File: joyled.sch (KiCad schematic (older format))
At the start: 16 parts, among them P3 GAMEPAD 2, P6 GAMEPAD 1, U1 VGA SYNC/JOY BUFFER, U7 BACKLIGHT COVER

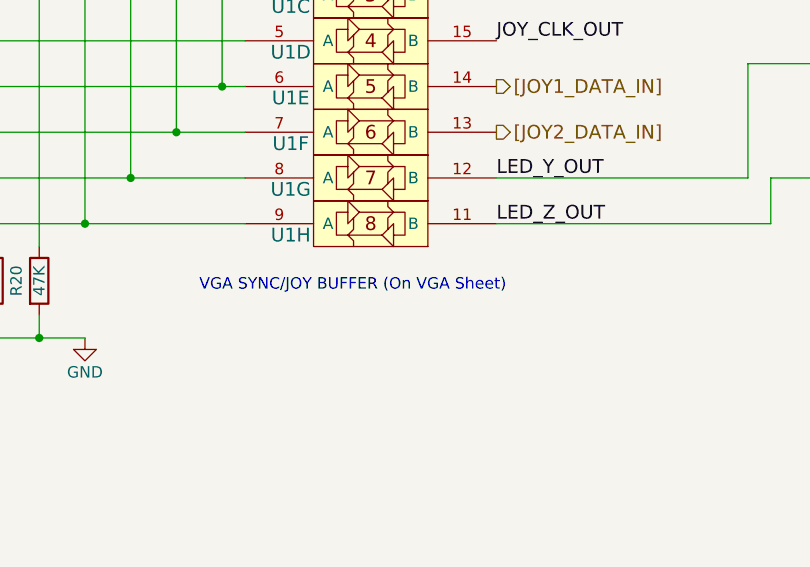
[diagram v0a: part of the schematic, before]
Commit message: Detalles menores (reordenamiento de labels, correccion de titulo, etc
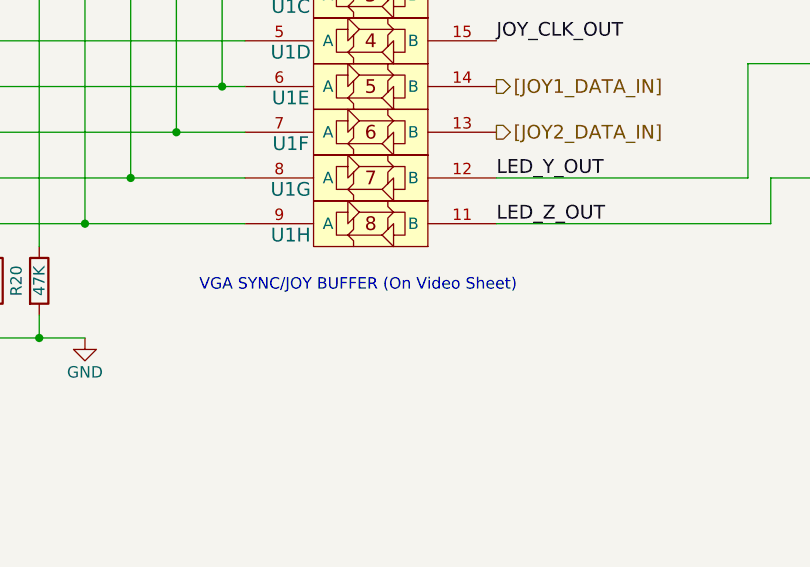
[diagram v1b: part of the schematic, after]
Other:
- note added: "VGA SYNC/JOY BUFFER (On Video Sheet)"
- note removed: "VGA SYNC/JOY BUFFER (On VGA Sheet)"
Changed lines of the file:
@@
 Connection ~ 2400 2600
 Text Notes 3300 3700 0    50   ~ 0
-VGA SYNC/JOY BUFFER (On VGA Sheet)
+VGA SYNC/JOY BUFFER (On Video Sheet)
 $Comp
 L DB9S_NES8 P3

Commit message: Cambios menores
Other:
- moved on the sheet: G3, G4
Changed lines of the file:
@@
 $EndComp
 $Comp
-L GND #PWR022
+L GND #PWR019
 U 1 1 5BD0B1F1
 P 2800 3900
-F 0 "#PWR022" H 2800 3650 50  0001 C CNN
+F 0 "#PWR019" H 2800 3650 50  0001 C CNN
 F 1 "GND" H 2800 3750 50  0000 C CNN
 F 2 "" H 2800 3900 50  0000 C CNN
@@
 $EndComp
 $Comp
-L +3.3V #PWR023
+L +3.3V #PWR020
 U 1 1 5BD0B1F7
 P 2200 1900
-F 0 "#PWR023" H 2200 1750 50  0001 C CNN
+F 0 "#PWR020" H 2200 1750 50  0001 C CNN
 F 1 "+3.3V" H 2200 2040 50  0000 C CNN
 F 2 "" H 2200 1900 50  0000 C CNN
@@
 LED_Z_OUT
 $Comp
-L +5V #PWR024
+L +5V #PWR021
 U 1 1 5BD0B238
 P 7400 2700
-F 0 "#PWR024" H 7400 2550 50  0001 C CNN
+F 0 "#PWR021" H 7400 2550 50  0001 C CNN
 F 1 "+5V" H 7400 2840 50  0000 C CNN
 F 2 "" H 7400 2700 50  0000 C CNN
@@
 $EndComp
 $Comp
-L +5V #PWR025
+L +5V #PWR022
 U 1 1 5BD0B23E
 P 7400 3200
-F 0 "#PWR025" H 7400 3050 50  0001 C CNN
+F 0 "#PWR022" H 7400 3050 50  0001 C CNN
 F 1 "+5V" H 7400 3340 50  0000 C CNN
 F 2 "" H 7400 3200 50  0000 C CNN
@@
 L INVADER_LOGO_BACK G3
 U 1 1 5BD0B291
-P 5225 5475
-F 0 "G3" H 5225 5650 60  0000 C CNN
-F 1 "LOGO BACKLIGHT" H 5225 5150 60  0000 C CNN
-F 2 "Salmon:TREX_LOGO_BACK" H 5225 5475 60  0001 C CNN
-F 3 "" H 5225 5475 60  0001 C CNN
-	1    5225 5475
+P 5725 5475
+F 0 "G3" H 5725 5650 60  0000 C CNN
+F 1 "LOGO BACKLIGHT" H 5725 5150 60  0000 C CNN
+F 2 "Salmon:TREX_LOGO_BACK" H 5725 5475 60  0001 C CNN
+F 3 "" H 5725 5475 60  0001 C CNN
+	1    5725 5475
 	1    0    0    -1
 $EndComp
@@
 L RETROCIAA_LOGO_BACK G4
 U 1 1 5BD0B298
-P 3850 5475
-F 0 "G4" H 3850 5650 60  0000 C CNN
-F 1 "RETRO-CIAA BACKLIGHT" H 3850 5150 60  0000 C CNN
-F 2 "Salmon:RETROCIAA_LOGO_BACK" H 3850 5475 60  0001 C CNN
-F 3 "" H 3850 5475 60  0001 C CNN
-	1    3850 5475
+P 4050 5475
+F 0 "G4" H 4050 5650 60  0000 C CNN
+F 1 "RETRO-CIAA BACKLIGHT" H 4050 5150 60  0000 C CNN
+F 2 "Salmon:RETROCIAA_LOGO_BACK" H 4050 5475 60  0001 C CNN
+F 3 "" H 4050 5475 60  0001 C CNN
+	1    4050 5475
 	1    0    0    -1
 $EndComp
@@
 NES 8 Bit (Family Game) Gamepads\nusing CMOS 4021 shift register.
 $Comp
-L Earth #PWR026
+L Earth #PWR023
 U 1 1 5BD0EAA8
 P 10500 4100
-F 0 "#PWR026" H 10500 3850 50  0001 C CNN
+F 0 "#PWR023" H 10500 3850 50  0001 C CNN
 F 1 "Earth" H 10500 3950 50  0001 C CNN
 F 2 "" H 10500 4100 50  0000 C CNN
@@
 $EndComp
 $Comp
-L Earth #PWR027
+L Earth #PWR024
 U 1 1 5BD0EAAE
 P 10500 2100
-F 0 "#PWR027" H 10500 1850 50  0001 C CNN
+F 0 "#PWR024" H 10500 1850 50  0001 C CNN
 F 1 "Earth" H 10500 1950 50  0001 C CNN
 F 2 "" H 10500 2100 50  0000 C CNN
@@
 [LED_Z]
 $Comp
-L GND #PWR028
+L GND #PWR025
 U 1 1 5BD2F9D4
 P 1700 5900
-F 0 "#PWR028" H 1700 5650 50  0001 C CNN
+F 0 "#PWR025" H 1700 5650 50  0001 C CNN
 F 1 "GND" H 1700 5750 50  0000 C CNN
 F 2 "" H 1700 5900 50  0000 C CNN
@@
 $EndComp
 $Comp
-L GND #PWR029
+L GND #PWR026
 U 1 1 5BD2FA3A
 P 2700 5900
-F 0 "#PWR029" H 2700 5650 50  0001 C CNN
+F 0 "#PWR026" H 2700 5650 50  0001 C CNN
 F 1 "GND" H 2700 5750 50  0000 C CNN
 F 2 "" H 2700 5900 50  0000 C CNN
@@
 3V3
 $Comp
-L +5V #PWR030
+L +5V #PWR027
 U 1 1 5BD5D879
 P 6100 7400
-F 0 "#PWR030" H 6100 7250 50  0001 C CNN
+F 0 "#PWR027" H 6100 7250 50  0001 C CNN
 F 1 "+5V" H 6100 7540 50  0000 C CNN
 F 2 "" H 6100 7400 50  0000 C CNN
@@
 $EndComp
 $Comp
-L +3.3V #PWR031
+L +3.3V #PWR028
 U 1 1 5BD5D87F
 P 5700 7400
-F 0 "#PWR031" H 5700 7250 50  0001 C CNN
+F 0 "#PWR028" H 5700 7250 50  0001 C CNN
 F 1 "+3.3V" H 5700 7540 50  0000 C CNN
 F 2 "" H 5700 7400 50  0000 C CNN
@@
 $EndComp
 $Comp
-L GND #PWR032
+L GND #PWR029
 U 1 1 5BD5D885
 P 6700 7400
-F 0 "#PWR032" H 6700 7150 50  0001 C CNN
+F 0 "#PWR029" H 6700 7150 50  0001 C CNN
 F 1 "GND" H 6700 7250 50  0000 C CNN
 F 2 "" H 6700 7400 50  0000 C CNN

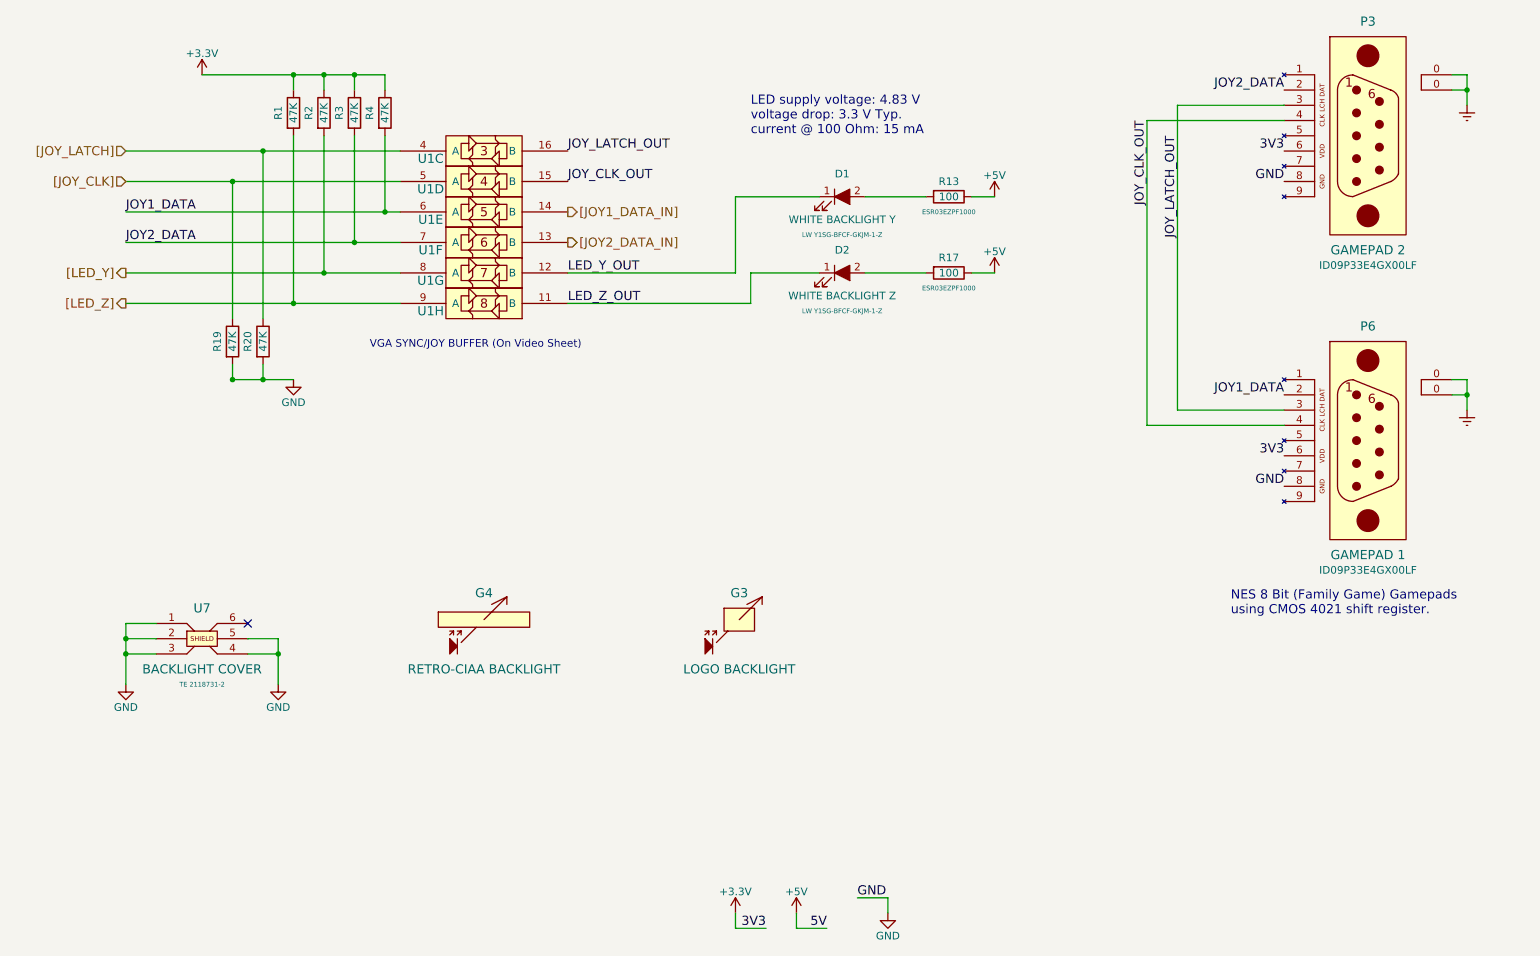
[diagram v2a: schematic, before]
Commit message: Nuevo layout, mejoras y modificaciones del revisor
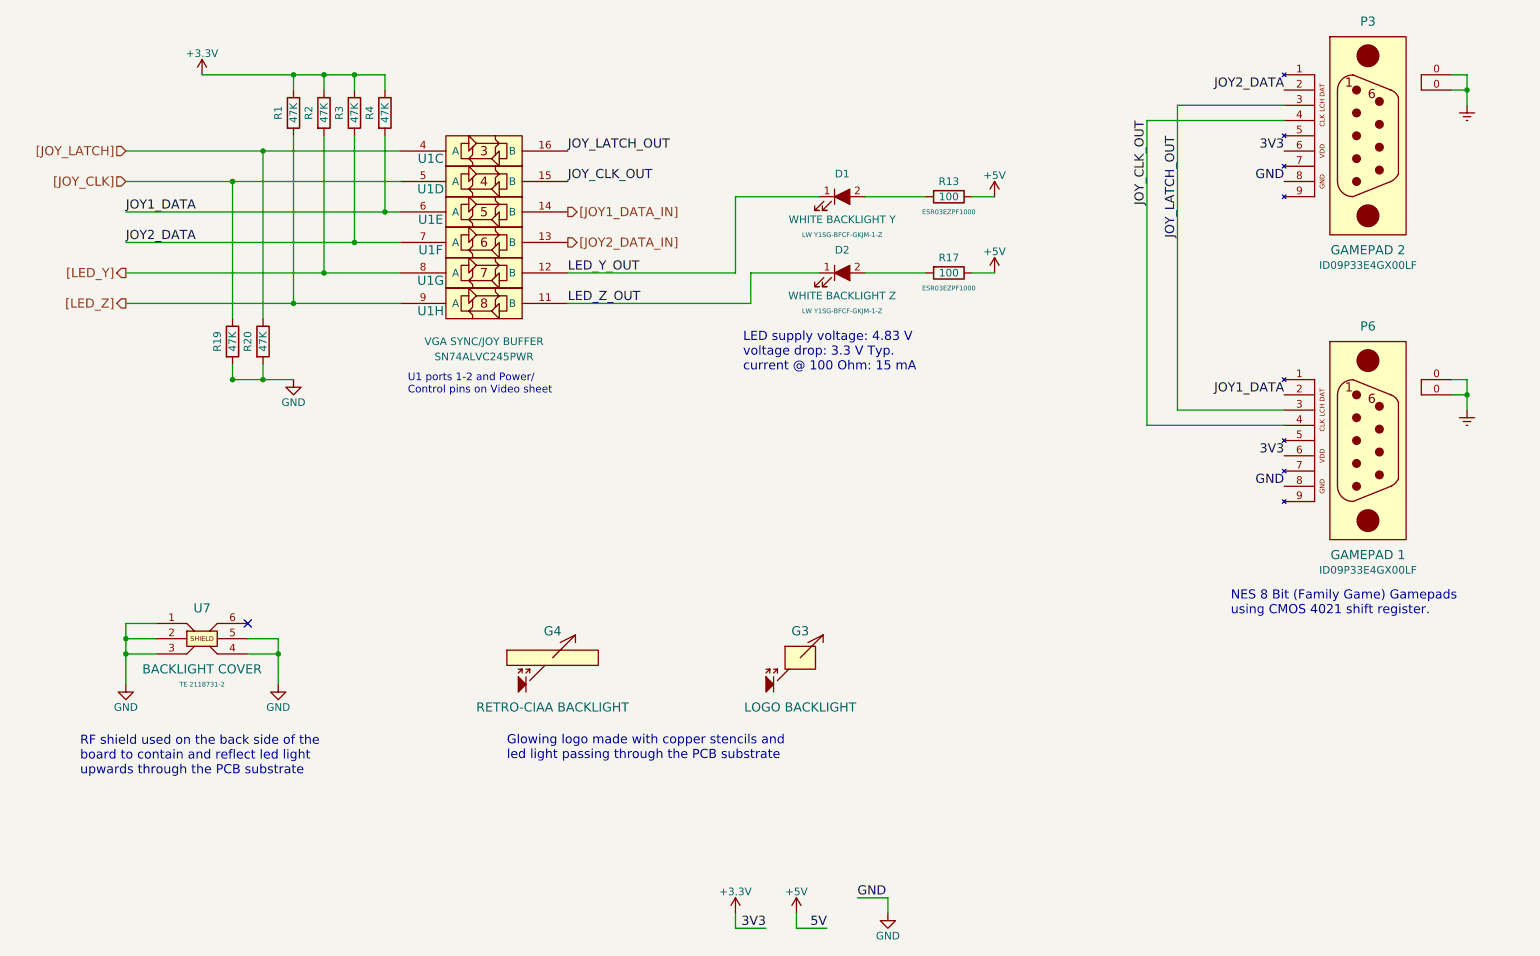
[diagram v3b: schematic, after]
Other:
- note added: "Glowing logo made with copper stencils and\nled light passing through the PCB substrate"
- note added: "RF shield used on the back side of the\nboard to contain and reflect led light \nupwards through the PCB substrate"
- note added: "U1 ports 1-2 and Power/\nControl pins on Video sheet"
- note removed: "VGA SYNC/JOY BUFFER (On Video Sheet)"
- moved on the sheet: G3, G4
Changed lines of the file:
@@
 LIBS:contrib
 LIBS:valves
-LIBS:salmon
+LIBS:retro-ciaa
 LIBS:retro-ciaa-cache
 EELAYER 25 0
@@
 encoding utf-8
 Sheet 3 8
-Title "RETRO-CIAA / JOYSTICKS & BACKLIGHT"
-Date "2018-10-19"
+Title "JOYSTICKS & BACKLIGHT"
+Date "2018-10-20"
 Rev "1.1.1"
-Comp "Salmon Robotics"
+Comp "http://www.retro-ciaa.com"
 Comment1 "All resistors 1% & 0603\" unless otherwise noted"
 Comment2 "ERC check OK on 2018-10-19"
@@
 L INVADER_LOGO_BACK G3
 U 1 1 5BD0B291
-P 5725 5475
-F 0 "G3" H 5725 5650 60  0000 C CNN
-F 1 "LOGO BACKLIGHT" H 5725 5150 60  0000 C CNN
-F 2 "Salmon:TREX_LOGO_BACK" H 5725 5475 60  0001 C CNN
-F 3 "" H 5725 5475 60  0001 C CNN
-	1    5725 5475
+P 6125 5725
+F 0 "G3" H 6125 5900 60  0000 C CNN
+F 1 "LOGO BACKLIGHT" H 6125 5400 60  0000 C CNN
+F 2 "Salmon:TREX_LOGO_BACK" H 6125 5725 60  0001 C CNN
+F 3 "" H 6125 5725 60  0001 C CNN
+	1    6125 5725
 	1    0    0    -1
 $EndComp
@@
 L RETROCIAA_LOGO_BACK G4
 U 1 1 5BD0B298
-P 4050 5475
-F 0 "G4" H 4050 5650 60  0000 C CNN
-F 1 "RETRO-CIAA BACKLIGHT" H 4050 5150 60  0000 C CNN
-F 2 "Salmon:RETROCIAA_LOGO_BACK" H 4050 5475 60  0001 C CNN
-F 3 "" H 4050 5475 60  0001 C CNN
-	1    4050 5475
+P 4500 5725
+F 0 "G4" H 4500 5900 60  0000 C CNN
+F 1 "RETRO-CIAA BACKLIGHT" H 4500 5400 60  0000 C CNN
+F 2 "Salmon:RETROCIAA_LOGO_BACK" H 4500 5725 60  0001 C CNN
+F 3 "" H 4500 5725 60  0001 C CNN
+	1    4500 5725
 	1    0    0    -1
 $EndComp
@@
 AR Path="/5BD08AB9/5BD0C08A" Ref="U1"  Part="8"
 F 0 "U1" H 3700 3350 60  0000 C CNN
-F 1 "VGA SYNC/JOY BUFFER" H 4050 3650 60  0001 C CNN
+F 1 "VGA SYNC/JOY BUFFER" H 4050 3150 50  0000 C CNN
 F 2 "" H 4050 3450 60  0001 C CNN
-F 3 "" H 4050 3450 60  0001 C CNN
+F 3 "SN74ALVC245PWR" H 4050 3050 50  0000 C CNN
 	8    4050 3400
 	1    0    0    -1
@@
 Connection ~ 2600 2400
 Connection ~ 2400 2600
-Text Notes 3300 3700 0    50   ~ 0
-VGA SYNC/JOY BUFFER (On Video Sheet)
+Text Notes 3550 4000 0    50   ~ 0
+U1 ports 1-2 and Power/\nControl pins on Video sheet
 $Comp
 L DB9S_NES8 P3
@@
 Wire Wire Line
 	10500 1900 10400 1900
-Text Notes 5800 2300 0    60   ~ 0
+Text Notes 5750 3850 0    60   ~ 0
 LED supply voltage: 4.83 V\nvoltage drop: 3.3 V Typ.\ncurrent @ 100 Ohm: 15 mA
 Text HLabel 1700 2400 0    60   Input ~ 0
@@
 Text HLabel 4600 3000 2    60   Output ~ 0
 [JOY2_DATA_IN]
+Text Notes 1400 6500 0    60   ~ 0
+RF shield used on the back side of the\nboard to contain and reflect led light \nupwards through the PCB substrate
+Text Notes 4200 6400 0    60   ~ 0
+Glowing logo made with copper stencils and\nled light passing through the PCB substrate
 $EndSCHEMATC

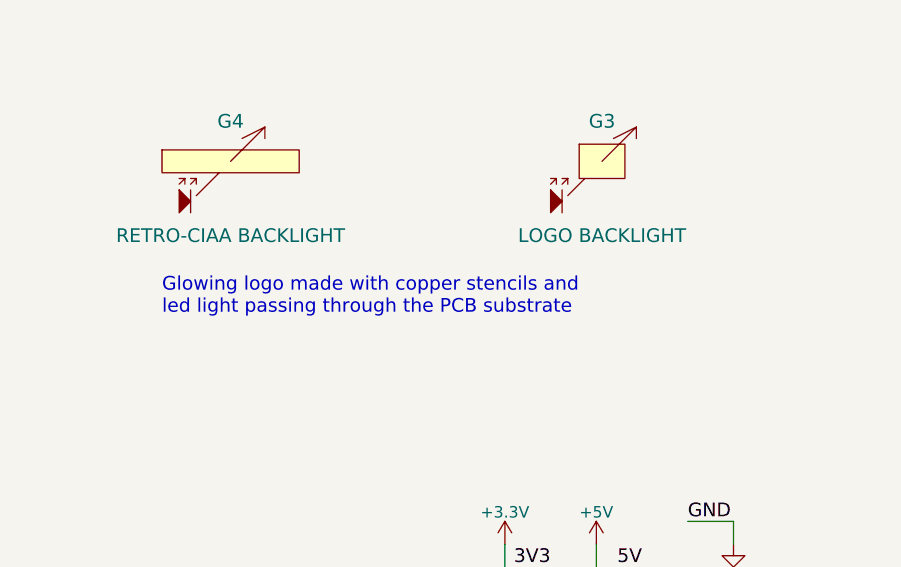
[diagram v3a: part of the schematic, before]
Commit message: Modificacion para clarificar uso de multiparte en U1 y U2
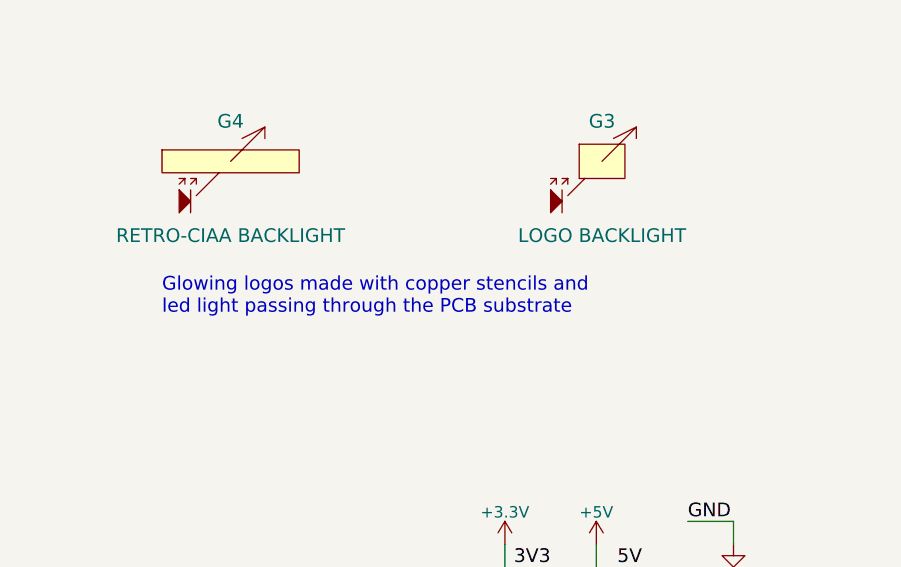
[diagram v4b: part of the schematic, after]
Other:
- note added: "Glowing logos made with copper stencils and\nled light passing through the PCB substrate"
- note removed: "Glowing logo made with copper stencils and\nled light passing through the PCB substrate"
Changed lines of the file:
@@
 EESchema Schematic File Version 2
-LIBS:retro-ciaa-rescue
 LIBS:power
 LIBS:device
@@
 RF shield used on the back side of the\nboard to contain and reflect led light \nupwards through the PCB substrate
 Text Notes 4200 6400 0    60   ~ 0
-Glowing logo made with copper stencils and\nled light passing through the PCB substrate
+Glowing logos made with copper stencils and\nled light passing through the PCB substrate
 $EndSCHEMATC

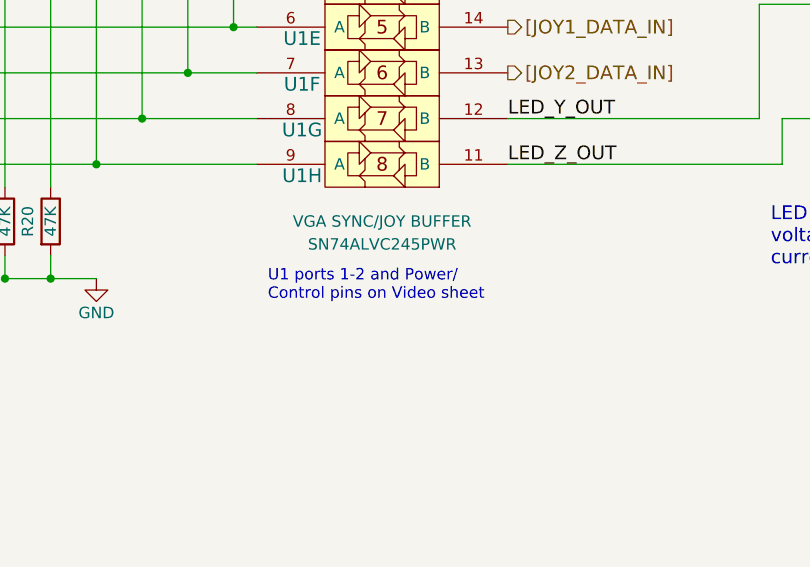
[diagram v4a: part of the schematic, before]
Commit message: Aclaracion menor sobre uso de U1 en diferentes sheets
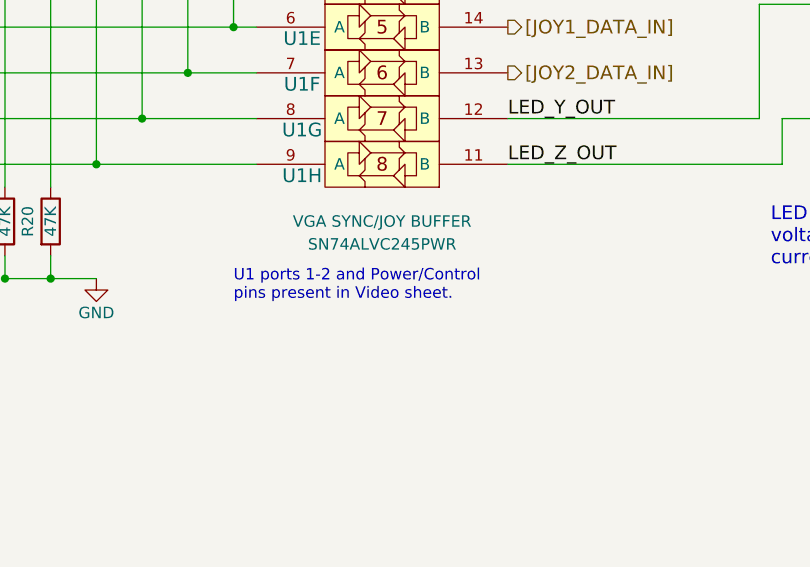
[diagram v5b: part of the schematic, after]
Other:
- note added: "U1 ports 1-2 and Power/Control\npins present in Video sheet."
- note removed: "U1 ports 1-2 and Power/\nControl pins on Video sheet"
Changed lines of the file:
@@
 Connection ~ 2600 2400
 Connection ~ 2400 2600
-Text Notes 3550 4000 0    50   ~ 0
-U1 ports 1-2 and Power/\nControl pins on Video sheet
+Text Notes 3400 4000 0    50   ~ 0
+U1 ports 1-2 and Power/Control\npins present in Video sheet.
 $Comp
 L DB9S_NES8 P3
